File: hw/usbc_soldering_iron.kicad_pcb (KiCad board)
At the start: 4 copper layers, 70 x 30 mm, 87 parts, among them J1 U263-163N-4OS1735, J16 TIP_CONN, J2 DBG, J3 OLED, J4 GPIO, J5 DISP, Q1 AGM403AP, U1 SC7A20, U10 TPA191Ax, U2 CH32X035F8U6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

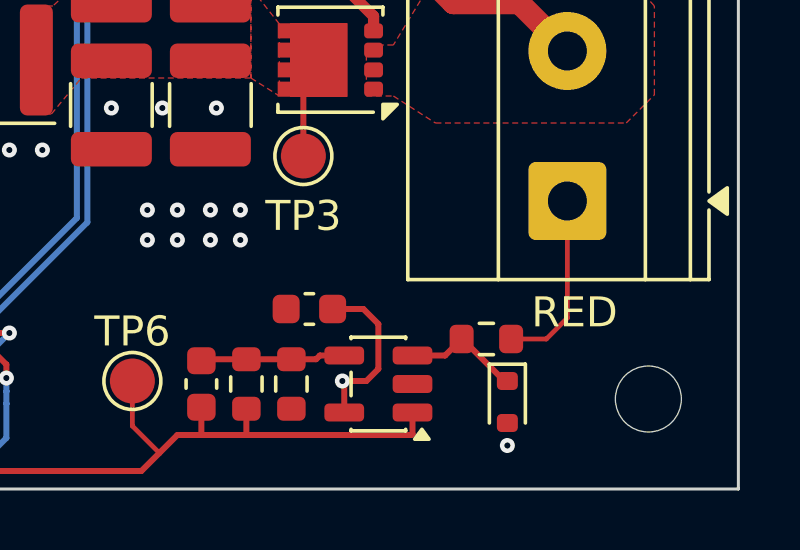
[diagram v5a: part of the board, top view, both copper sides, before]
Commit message: better protection diode for tlv333
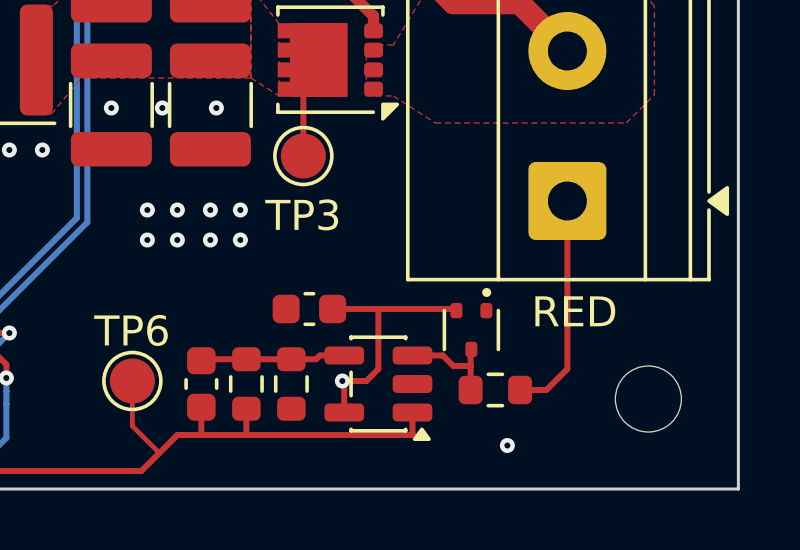
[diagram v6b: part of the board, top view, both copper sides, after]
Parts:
- removed D2: 3.3V, Diode_SMD:D_SOD-523
- added D1: BAV199T, Package_TO_SOT_SMD:SOT-523, F.Cu at (161.6, 152.9)
- moved R8 1.73 mm to (162.4, 154.9)
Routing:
- net +3.3V: track 187.1 -> 190.1 mm
- net /RED: track 6.06 -> 7.46 mm
- net Net-(D1-common): track 3.97 -> 3.45 mm

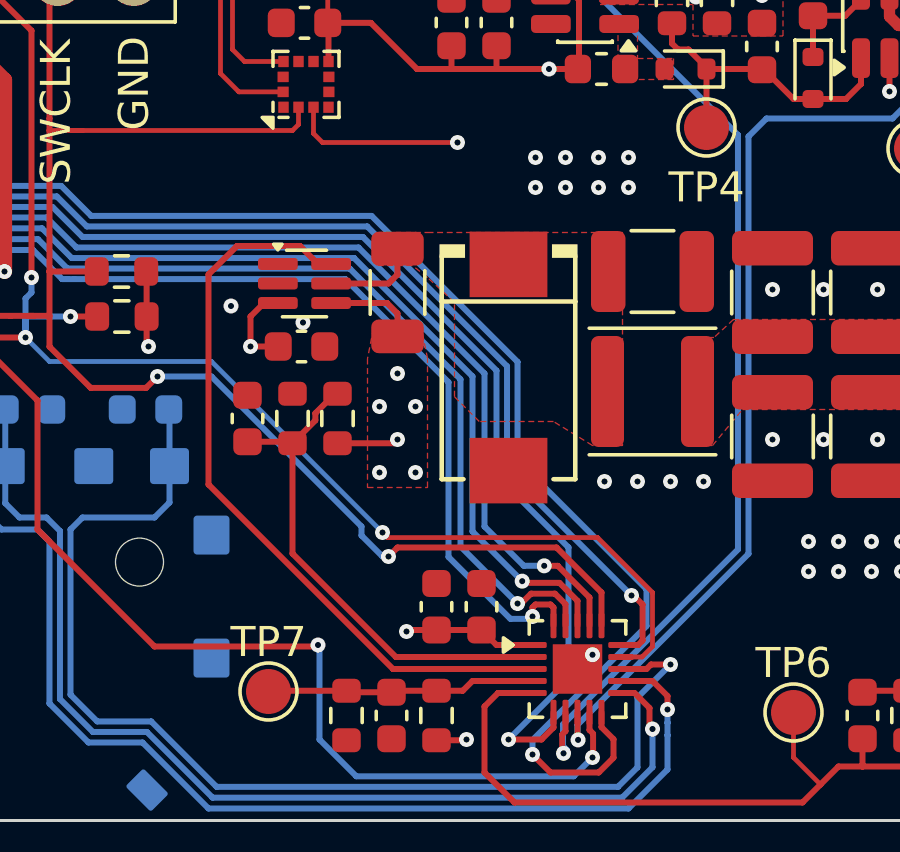
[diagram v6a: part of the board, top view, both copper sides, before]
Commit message: new footprint for big inductor
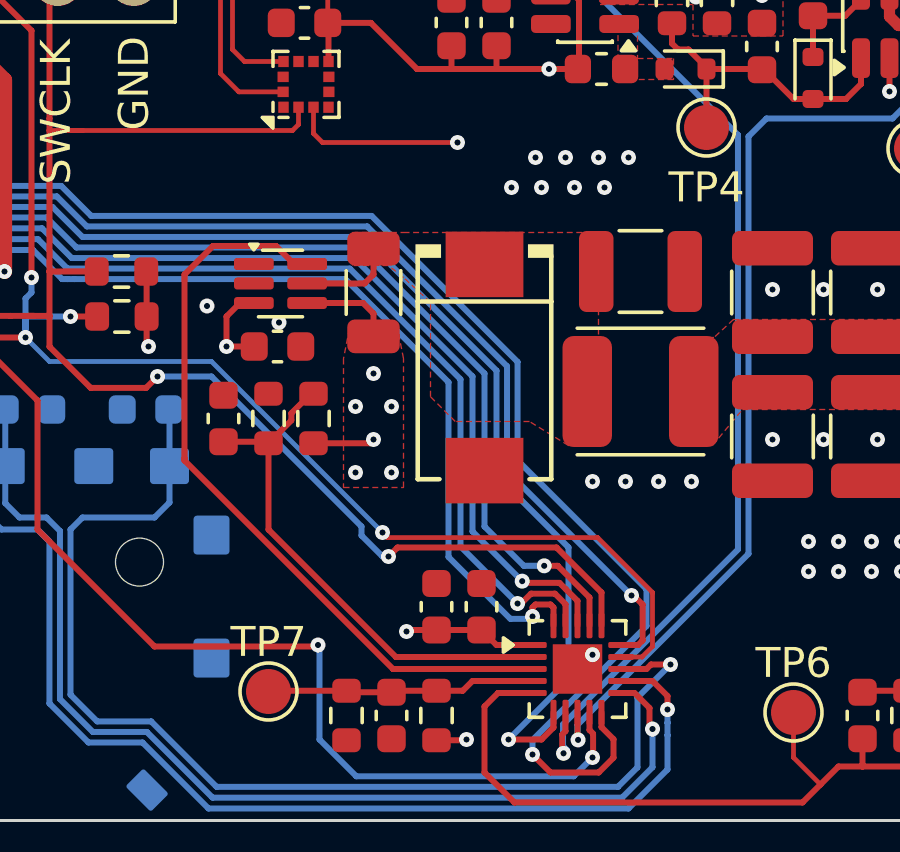
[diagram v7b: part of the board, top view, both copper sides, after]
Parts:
- L2: footprint Inductor_SMD:L_Changjiang_FNR4030S -> Custom:L_Changjiang_FNR4030S_Handsolder
- moved C12 0.80 mm to (133.1, 142.4)
- moved C13 0.80 mm to (140.0, 143.1)
- moved U10 0.80 mm to (133.2, 140.3)
- moved C27 0.80 mm to (131.3, 144.8)
- moved R11 0.80 mm to (136.3, 140.6)
- moved R16 0.80 mm to (134.3, 144.8)
- moved R17 0.80 mm to (132.8, 144.8)
- moved C15 0.40 mm to (145.2, 139.9)
- moved L2 0.40 mm to (145.2, 143.9)

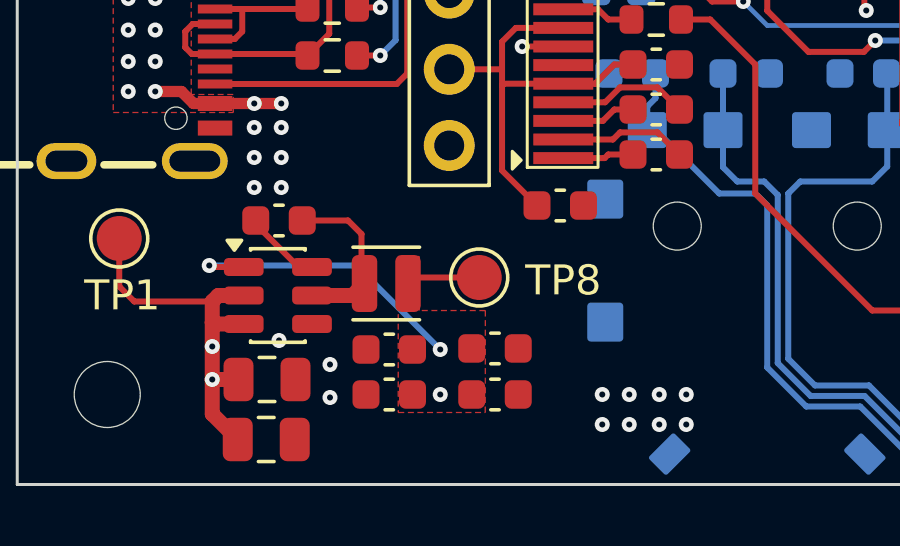
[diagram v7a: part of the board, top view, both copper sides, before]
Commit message: different inductor
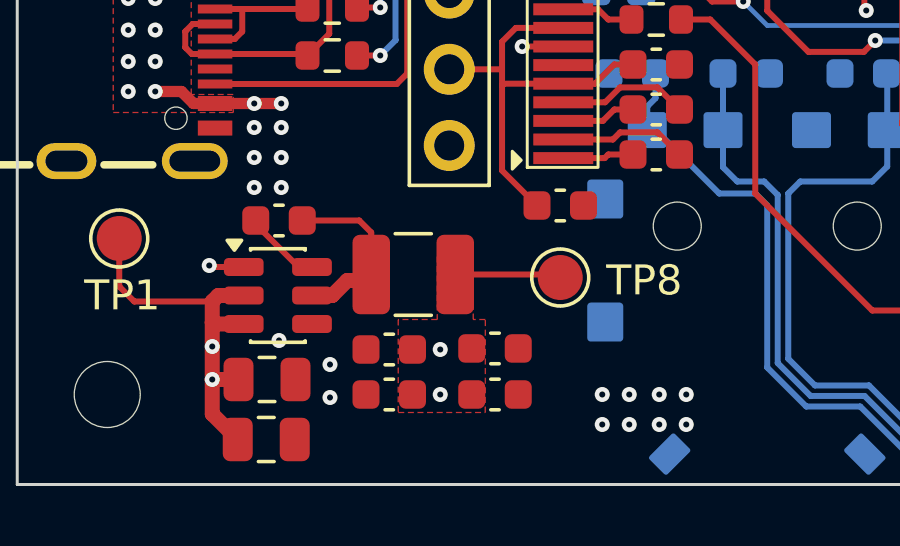
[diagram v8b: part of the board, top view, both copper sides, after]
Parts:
- L1: value 6.8u -> 22u; footprint Inductor_SMD:L_Wuerth_MAPI-2010 -> Inductor_SMD:L_1210_3225Metric
- R6: value 10k -> 10k 0.1%
- moved TP8 2.70 mm to (118.6, 151.3)
- moved L1 0.95 mm to (113.7, 151.2)
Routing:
- net +3.3V: track 190.1 -> 191.4 mm
- net Net-(U5-SW): track 5.53 -> 6.54 mm
